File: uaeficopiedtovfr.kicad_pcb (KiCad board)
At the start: 2 copper layers, 160 x 75.1 mm, 65 parts, among them J1 DTF13-12PB, J4 DTF13-12PB, J9 USB_C_Receptacle_USB2.0, M1 Module-power_12and5V-0.2, M2 Module-knock-0.2, M3 Module-vr-discrete-0.4, M4 Module-vr-max9924-0.1, M5 Module-wbo-0.5, M6 Module:mega-mcu100/0.2, M7 Module-wbo-0.5, P3 Pad, P4 Pad, Q1 ISL9V3040D3S, Q10 ZXMS6005SGTA, Q11 AO3400A, Q12 AO3400A, Q13 ZXMS6005SGTA, Q14 ZXMS6005SGTA, Q15 ZXMS6005SGTA, Q16 ZXMS6005SGTA, Q2 ISL9V3040D3S, Q3 ISL9V3040D3S, Q4 ISL9V3040D3S, Q7 ZXMS6005SGTA, Q8 ZXMS6005SGTA, Q9 ZXMS6005SGTA, U2 JDY-33

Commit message: Update uaeficopiedtovfr.kicad_pcb
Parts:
- added REF**: trollfaceVFR, Customparts:trollfaceVFR, F.Cu at (218.0, 120.4)

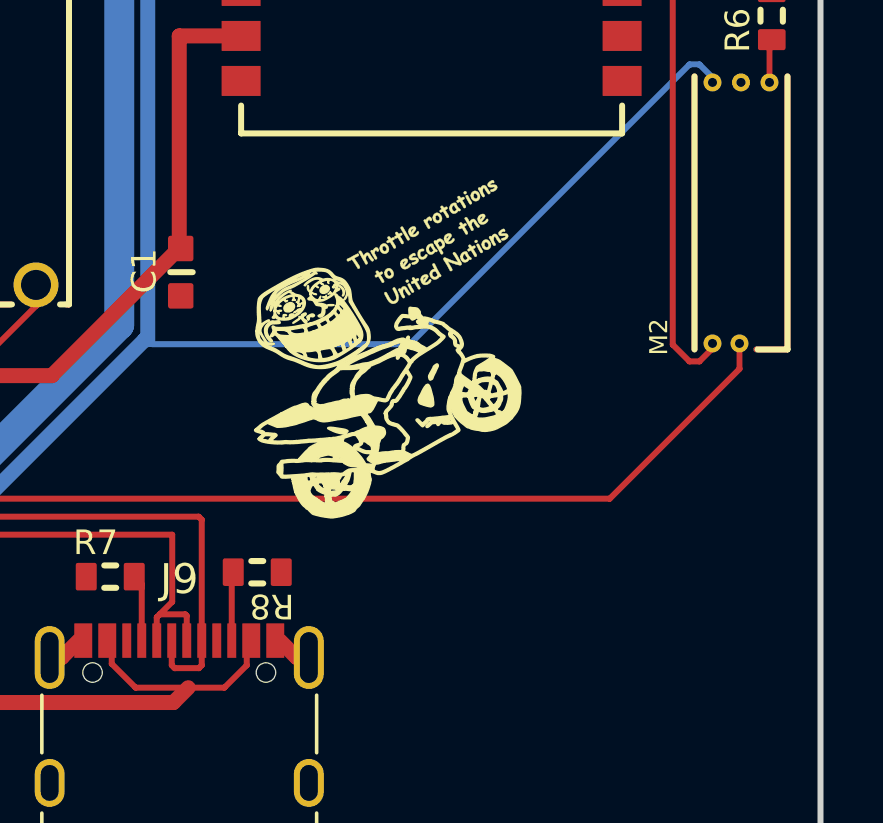
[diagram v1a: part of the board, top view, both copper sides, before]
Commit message: Re-added graphics to board
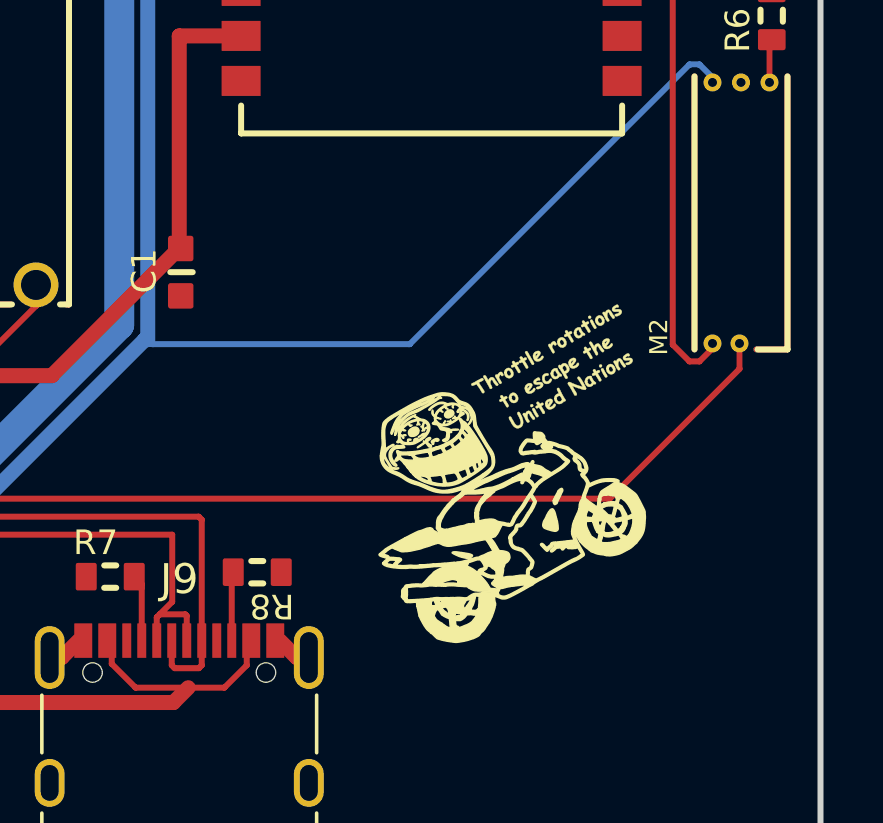
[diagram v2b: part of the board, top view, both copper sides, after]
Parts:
- moved REF** 5.87 mm to (222.1, 124.6)
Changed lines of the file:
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@@
   )
   (footprint "Customparts:trollfaceVFR" (layer "F.Cu")
-    (at 217.987855 120.422501)
+    (at 222.137855 124.572501)
     (fp_text reference "REF**" (at 0 -0.5 unlocked) (layer "F.SilkS") hide
         (effects (font (size 1 1) (thickness 0.1)))

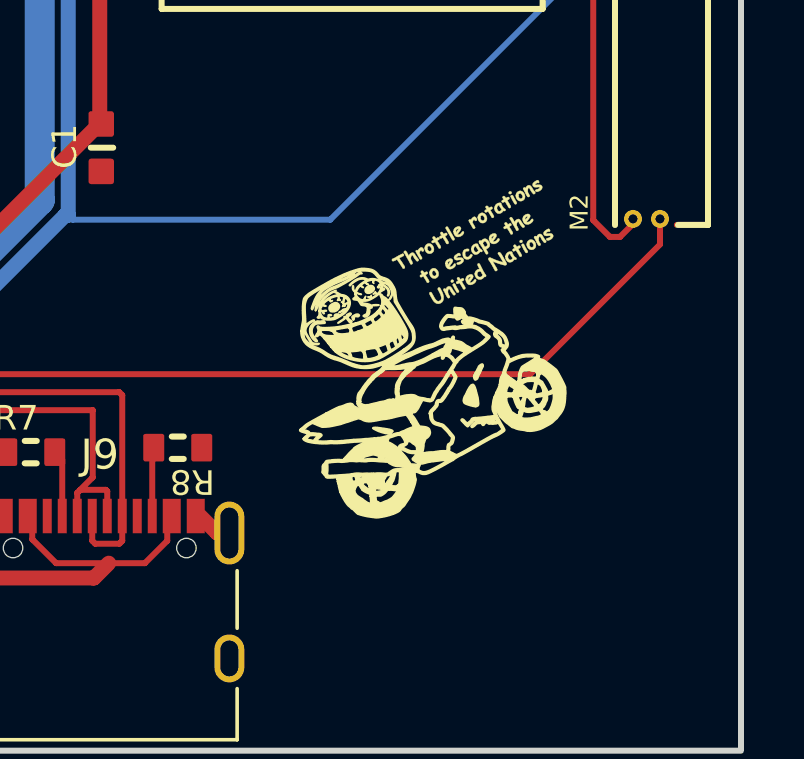
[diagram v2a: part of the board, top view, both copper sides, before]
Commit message: added ref to graphics
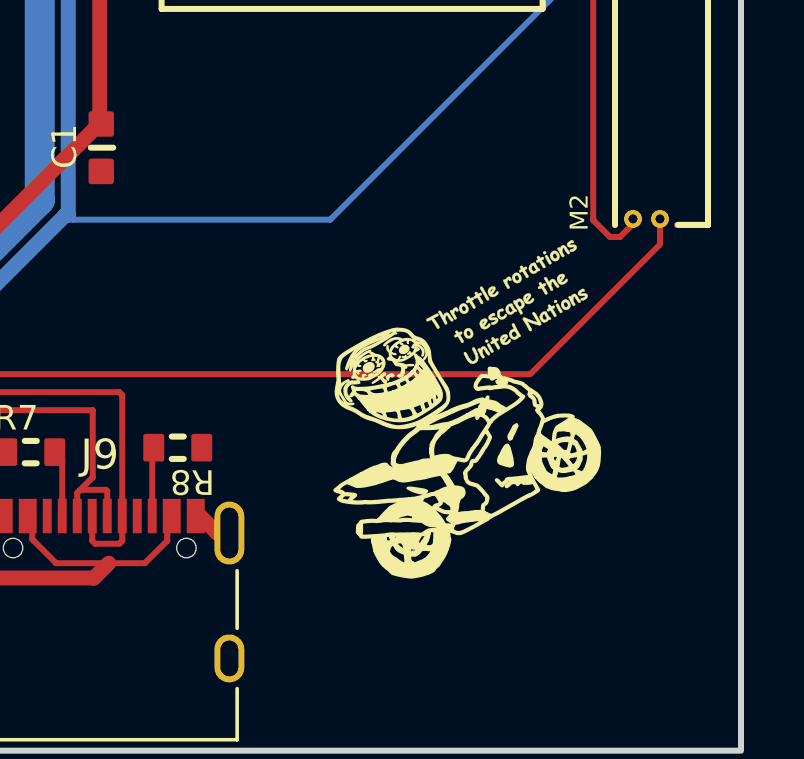
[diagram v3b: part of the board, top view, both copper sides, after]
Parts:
- removed REF**: trollfaceVFR, Customparts:trollfaceVFR
- added text1: ~, Customparts:trollfaceVFR, F.Cu at (223.3, 126.6)
